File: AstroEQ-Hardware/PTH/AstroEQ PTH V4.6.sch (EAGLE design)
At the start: 56 parts, among them IC1 ATMEGA162-16PU, IC2 PIC18F14K50-I/P, IC3 78L05, J1 POWER_JACKPTH, M1 Motor Driver, M2 Motor Driver, Q1 BS270, X1 16MHz, X2 12MHz

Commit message: Update AstroEQ PTH/SMD Schematics
1. Tidy up the schematics, add a frame, and improve labelling of nets
2. Add extra textual documentation to the PCB to label the various extra IO pins.
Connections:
- net MISO renamed IO3-MISO
- net MOSI renamed ESTOP-MOSI
- net SCLK renamed STAT-SCLK
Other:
- moved on the sheet: C1, C10, C11, C12, C13, C14, C15, C2, C3, C4, C5, C6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

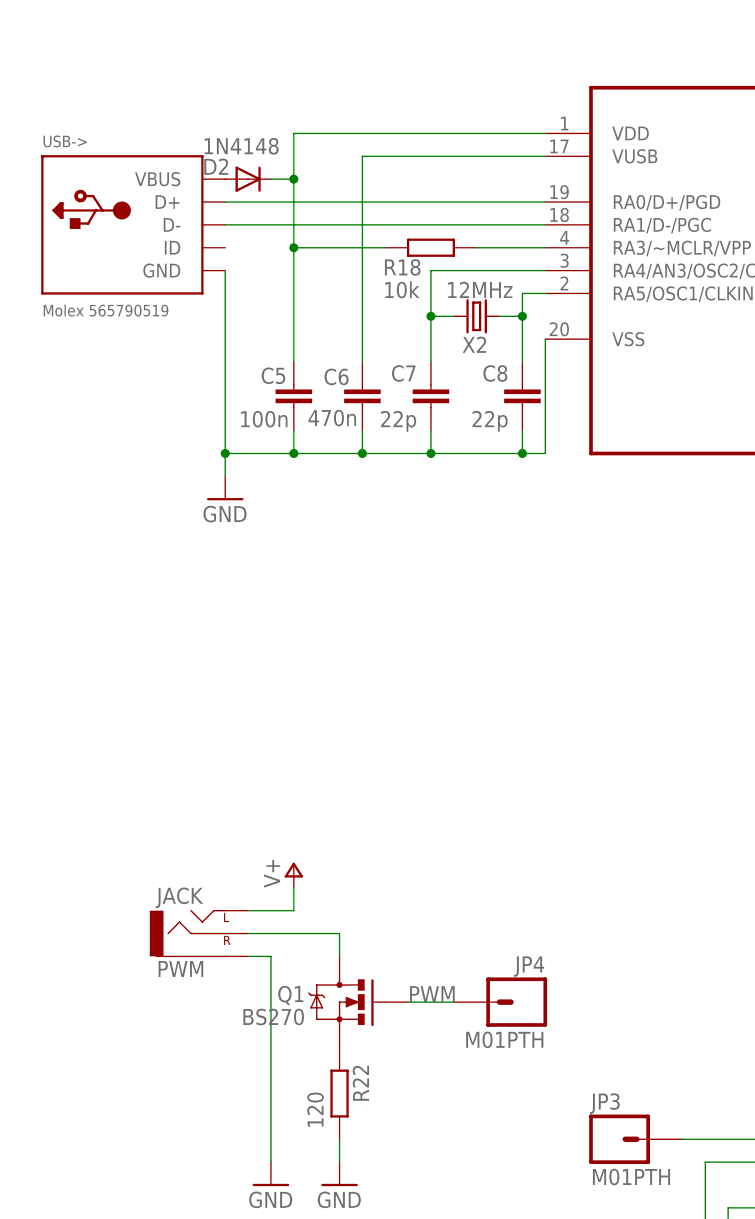
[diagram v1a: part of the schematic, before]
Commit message: Update PTH V4.6 design missing USB connector shell connections
The USB connector shell pins were not being joined to the GND planes.
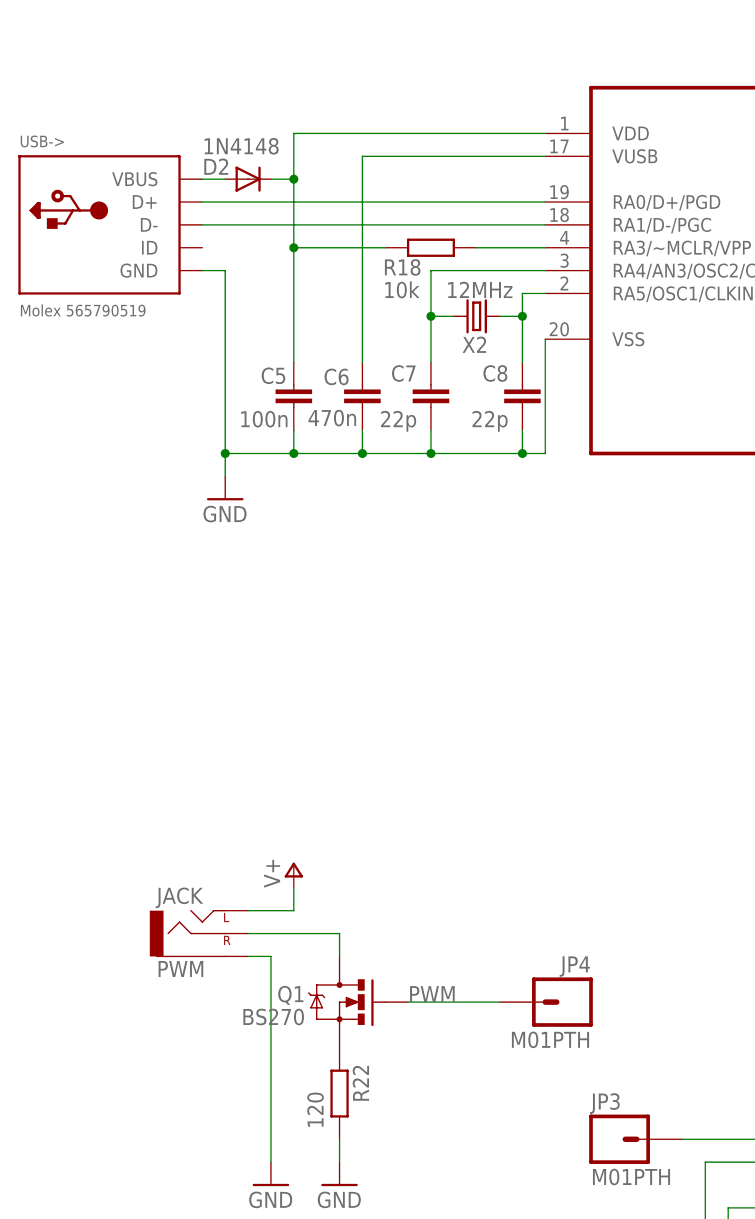
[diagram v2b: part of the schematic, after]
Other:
- moved on the sheet: JP4, USB->
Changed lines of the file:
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@@
 <attribute name="MPN" x="91.44" y="119.38" size="1.778" layer="96" display="off"/>
 </instance>
-<instance part="JP4" gate="G$1" x="81.28" y="134.62" rot="MR0">
-<attribute name="OC_FARNELL" x="81.28" y="134.62" size="1.778" layer="96" display="off"/>
-<attribute name="MF" x="81.28" y="134.62" size="1.778" layer="96" display="off"/>
-<attribute name="MPN" x="81.28" y="134.62" size="1.778" layer="96" display="off"/>
+<instance part="JP4" gate="G$1" x="86.36" y="134.62" rot="MR0">
+<attribute name="OC_FARNELL" x="86.36" y="134.62" size="1.778" layer="96" display="off"/>
+<attribute name="MF" x="86.36" y="134.62" size="1.778" layer="96" display="off"/>
+<attribute name="MPN" x="86.36" y="134.62" size="1.778" layer="96" display="off"/>
 </instance>
 <instance part="P+4" gate="1" x="55.88" y="149.86"/>
@@
 </instance>
 <instance part="P+10" gate="1" x="337.82" y="233.68"/>
-<instance part="USB-&gt;" gate="G$1" x="38.1" y="220.98">
-<attribute name="OC_FARNELL" value="1125347" x="38.1" y="220.98" size="1.778" layer="96" display="off"/>
-<attribute name="MF" value="MOLEX" x="38.1" y="220.98" size="1.778" layer="96" display="off"/>
-<attribute name="MPN" value="565790519" x="38.1" y="220.98" size="1.778" layer="96" display="off"/>
+<instance part="USB-&gt;" gate="G$1" x="35.56" y="220.98">
+<attribute name="OC_FARNELL" value="1125347" x="35.56" y="220.98" size="1.778" layer="96" display="off"/>
+<attribute name="MF" value="MOLEX" x="35.56" y="220.98" size="1.778" layer="96" display="off"/>
+<attribute name="MPN" value="565790519" x="35.56" y="220.98" size="1.778" layer="96" display="off"/>
 </instance>
 <instance part="C6" gate="G$1" x="63.5" y="200.66" smashed="yes" rot="R180">
@@
 <pinref part="IC2" gate="A" pin="VSS"/>
 <pinref part="USB-&gt;" gate="G$1" pin="GND"/>
+<wire x1="45.72" y1="215.9" x2="48.26" y2="215.9" width="0.1524" layer="91"/>
 <wire x1="48.26" y1="215.9" x2="48.26" y2="195.58" width="0.1524" layer="91"/>
 <wire x1="48.26" y1="195.58" x2="55.88" y2="195.58" width="0.1524" layer="91"/>
@@
 <label x="68.58" y="134.62" size="1.778" layer="95"/>
 <pinref part="Q1" gate="G$1" pin="G"/>
-<wire x1="68.58" y1="134.62" x2="73.66" y2="134.62" width="0.1524" layer="91"/>
+<wire x1="68.58" y1="134.62" x2="78.74" y2="134.62" width="0.1524" layer="91"/>
 </segment>
 </net>
@@
 <pinref part="USB-&gt;" gate="G$1" pin="D-"/>
 <pinref part="IC2" gate="A" pin="RA1/D-/PGC"/>
-<wire x1="48.26" y1="220.98" x2="83.82" y2="220.98" width="0.1524" layer="91"/>
+<wire x1="45.72" y1="220.98" x2="83.82" y2="220.98" width="0.1524" layer="91"/>
 </segment>
 </net>
@@
 <pinref part="USB-&gt;" gate="G$1" pin="D+"/>
 <pinref part="IC2" gate="A" pin="RA0/D+/PGD"/>
-<wire x1="83.82" y1="223.52" x2="48.26" y2="223.52" width="0.1524" layer="91"/>
+<wire x1="83.82" y1="223.52" x2="45.72" y2="223.52" width="0.1524" layer="91"/>
 </segment>
 </net>
@@
 <pinref part="USB-&gt;" gate="G$1" pin="VBUS"/>
 <pinref part="D2" gate="G$1" pin="A"/>
-</segment>
-</net>
+<wire x1="45.72" y1="226.06" x2="48.26" y2="226.06" width="0.1524" layer="91"/>
+</segment>
+</net>
